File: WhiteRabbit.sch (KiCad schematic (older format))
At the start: 52 parts, among them U13 LP5951MF-3.0/NOPB, U14 LM336M-2.5, U16 AD5662BRMZ-1, U19 AD5662BRMZ-1, U20 CDCM61004RHBT, Y1 OSC_25MHZ_RAKON_IVT3205CR, Y2 VM53S3-25.000-2.5/-30+75, Y3 OSC_20MHZ_IQD_LFVCXO026156

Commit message: DDR terminations changed, HTML BoM with variant added
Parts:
- removed R101, R102, R95, R96, R97, R98, R99: DNP, Resistors SMD:RESC1005X40N, symbol AMC_FMC_Carrier-PcbDoc-rescue:R-Device
- added R101, R102, R95, R96, R97, R98, R99: R0402_0R_JUMPER, RESC1005X40N, symbol Resistors_SMD:R0402_0R_JUMPER
- Y1: config (none) -> dnf

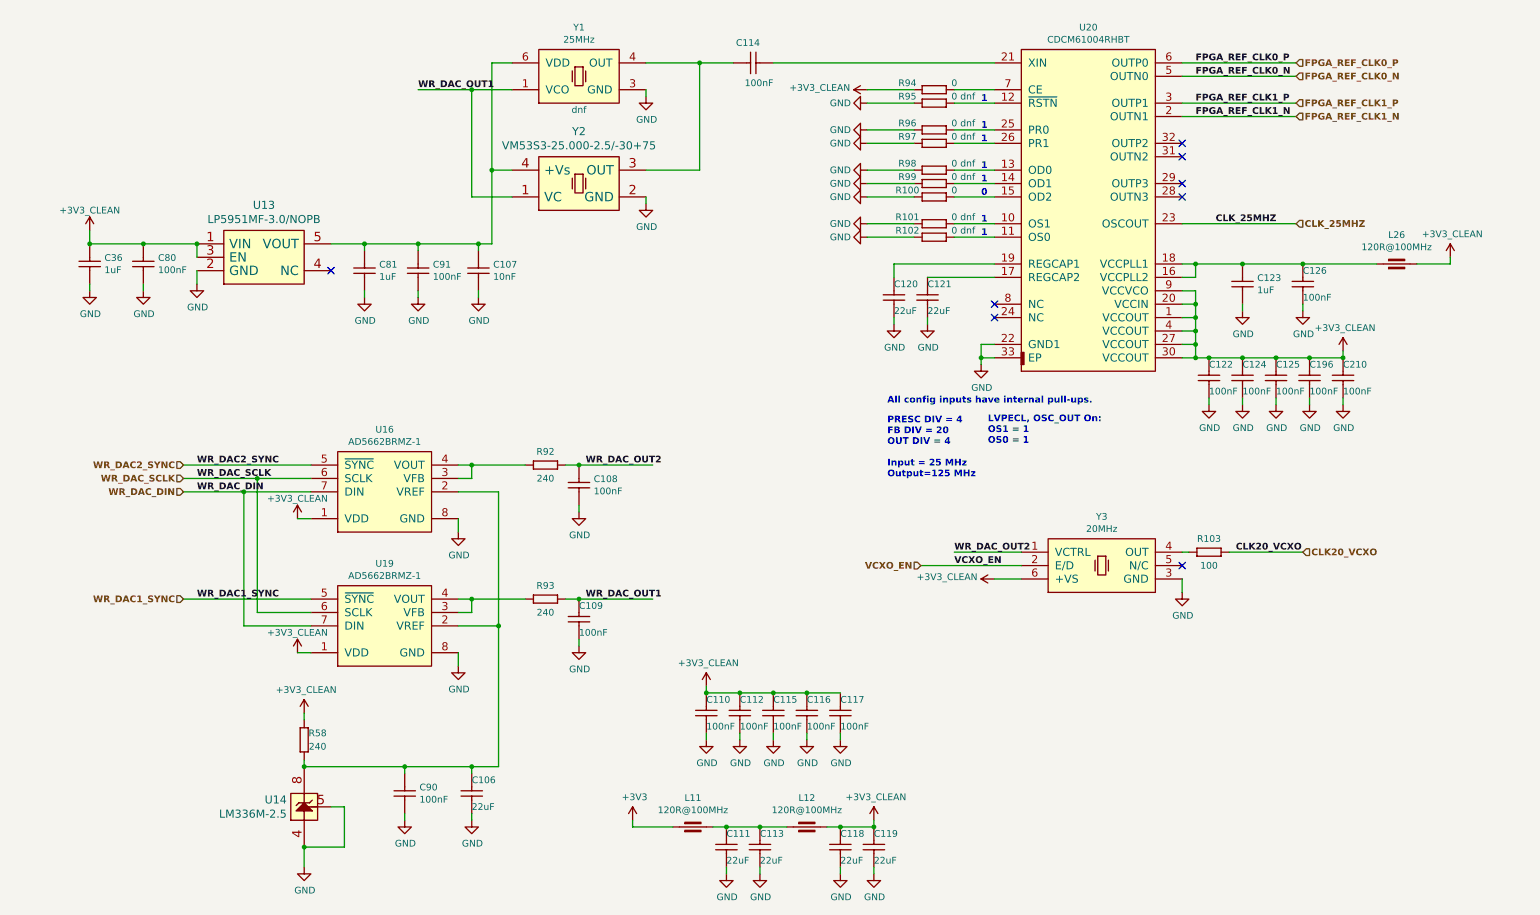
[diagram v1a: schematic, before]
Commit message: SW2 placement changed, BOM cleared, FPGA boot, less ERC errors and wornings
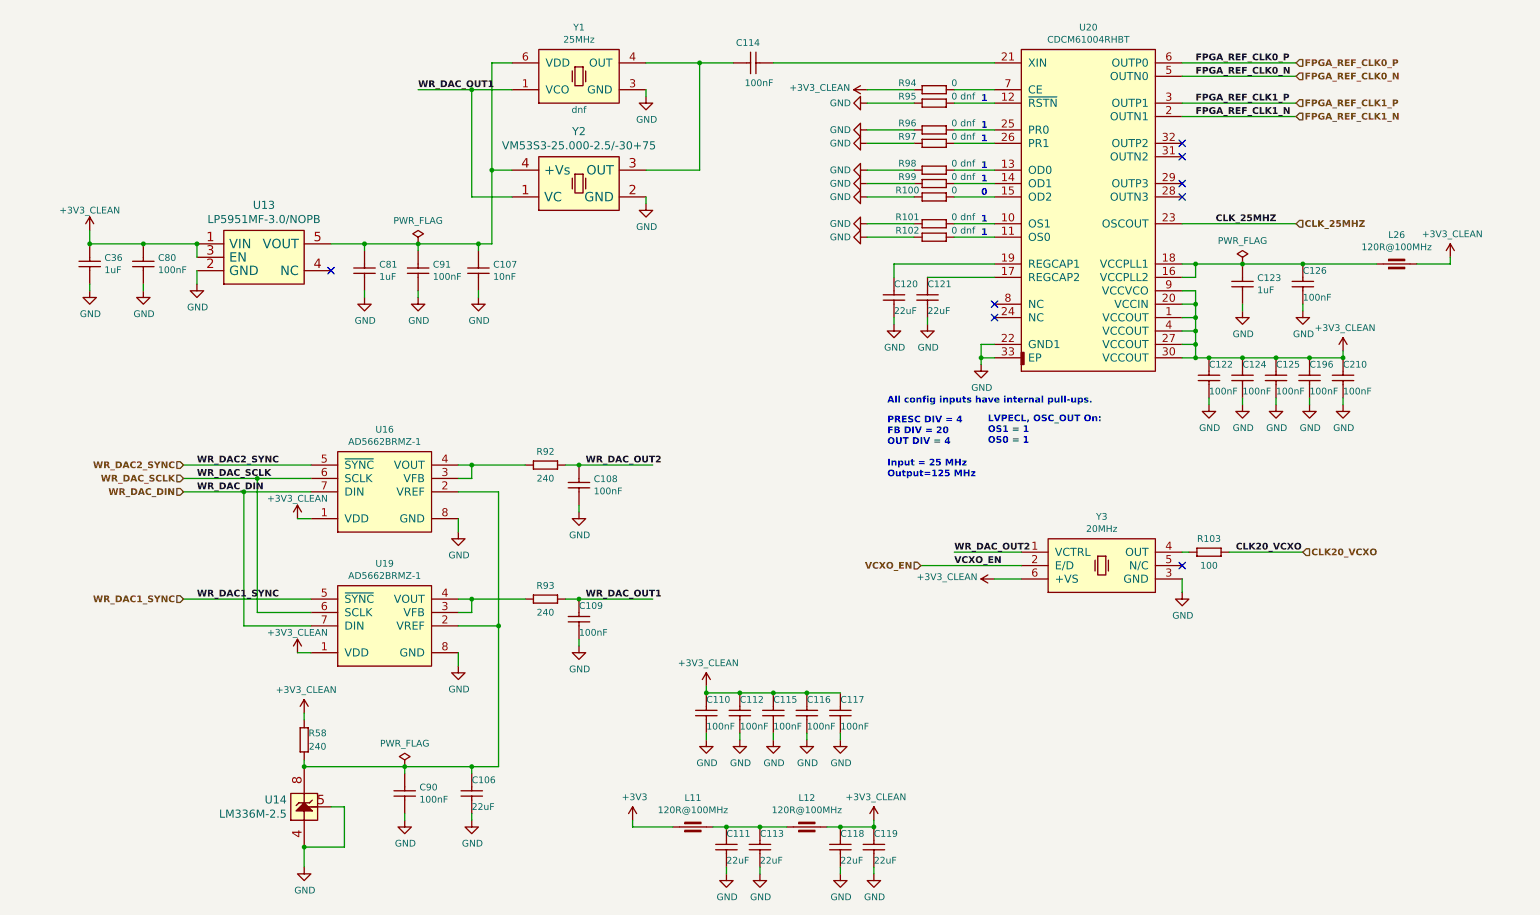
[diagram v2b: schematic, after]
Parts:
- U19: footprint SOP65P490X110-8N -> ICs And Semiconductors SMD:SOP65P490X110-8N
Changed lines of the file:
@@
-$EndComp
-$Comp
-L Analog_&_Interface:AD5662BRMZ-1 U19
-U 1 1 5C5A41A5
-P 2550 5150
-F 0 "U19" H 2900 5315 50  0000 C CNN
-F 1 "AD5662BRMZ-1" H 2900 5224 50  0000 C CNN
-F 2 "SOP65P490X110-8N" H 2550 3460 60  0001 L CNN
-F 3 "\\\\cern.ch\\dfs\\Applications\\Altium\\Datasheets\\AD5662BRMZ-1.pdf" H 2550 4180 60  0001 L CNN
-F 4 "AD5662BRMZ-1" H 2550 4090 60  0001 L CNN "Part Number"
-F 5 "AD5662" H 2550 4000 60  0001 L CNN "Library Ref"
-F 6 "SchLib\\Analog & Interface.SchLib" H 2550 3910 60  0001 L CNN "Library Path"
-F 7 "=Device" H 2550 3820 60  0001 L CNN "Comment"
-F 8 "Standard" H 2550 3730 60  0001 L CNN "Component Kind"
-F 9 "Standard" H 2550 3640 60  0001 L CNN "Component Type"
-F 10 "AD5662BRMZ-1" H 2550 3550 60  0001 L CNN "Device"
-F 11 "SOP, 0.65mm, Pitch; 8 Pin, 3.0mm W X 3.0mm L X 1.10mm H Body, IPC Medium Density" H 2550 3370 60  0001 L CNN "PackageDescription"
-F 12 "~~" H 2550 3280 60  0001 L CNN "Status"
-F 13 "2.7V to 5.5V, 250uA, Rail-to-Rail Output 16-Bit nanoDAC" H 2550 3190 60  0001 L CNN "Part Description"
-F 14 "ANALOG DEVICES" H 2550 3100 60  0001 L CNN "Manufacturer"
-F 15 "AD5662BRMZ-1" H 2550 3010 60  0001 L CNN "Manufacturer Part Number"
-F 16 "8" H 2550 2920 60  0001 L CNN "Pin Count"
-F 17 "MSOP8" H 2550 2830 60  0001 L CNN "Case"
-F 18 "Yes" H 2550 2740 60  0001 L CNN "Mounted"
-F 19 "No" H 2550 2650 60  0001 L CNN "Socket"
-F 20 "Yes" H 2550 2560 60  0001 L CNN "SMD"
-F 21 "No" H 2550 2470 60  0001 L CNN "PressFit"
-F 22 "No" H 2550 2380 60  0001 L CNN "Sense"
-F 23 "~~" H 2550 2290 60  0001 L CNN "Sense Comment"
-F 24 "No" H 2550 2200 60  0001 L CNN "Bonding"
-F 25 "~~" H 2550 2110 60  0001 L CNN "Status Comment"
-F 26 "1.1mm" H 2550 2020 60  0001 L CNN "ComponentHeight"
-F 27 "PcbLib\\ICs And Semiconductors SMD.PcbLib" H 2550 1930 60  0001 L CNN "Footprint Path"
-F 28 "SOP65P490X110-8N" H 2550 1840 60  0001 L CNN "Footprint Ref"
-F 29 "CERN DEM JLC" H 2550 1750 60  0001 L CNN "Author"
-F 30 "\\\\cern.ch\\dfs\\Applications\\Altium\\Datasheets\\AD5662BRMZ-1.pdf" H 2550 1660 60  0001 L CNN "HelpURL"
-F 31 "~~" H 2550 1570 60  0001 L CNN "ComponentLink1URL"
-F 32 "~~" H 2550 1480 60  0001 L CNN "ComponentLink2URL"
-F 33 "~~" H 2550 1390 60  0001 L CNN "ComponentLink2Description"
-F 34 "~~" H 2550 1300 60  0001 L CNN "ComponentLink1Description"
-F 35 "01/10/11 00:00:00" H 2550 1210 60  0001 L CNN "CreateDate"
-F 36 "01/10/11 00:00:00" H 2550 1120 60  0001 L CNN "LatestRevisionDate"
-F 37 "ICs And Semiconductors SMD" H 2550 1030 60  0001 L CNN "Library Name"
-F 38 "This work is licensed under the Creative Commons CC-BY-SA 4.0 License. To the extent that circuit schematics that use Licensed Material can be considered to be ‘Adapted Material’, then the copyright holder waives article 3.b of the license with respect to these schematics." H 2550 940 60  0001 L CNN "License"
-	1    2550 5150
-	1    0    0    -1
 $EndComp
 $Comp
@@
 	1    0    0    -1
 $EndComp
+$Comp
+L power:PWR_FLAG #FLG?
+U 1 1 5D1ECBBF
+P 3150 2600
+AR Path="/5BABAC65/5D1ECBBF" Ref="#FLG?"  Part="1"
+AR Path="/5C16BF13/5D1ECBBF" Ref="#FLG0113"  Part="1"
+F 0 "#FLG0113" H 3150 2675 50  0001 C CNN
+F 1 "PWR_FLAG" H 3150 2773 50  0000 C CNN
+F 2 "" H 3150 2600 50  0001 C CNN
+F 3 "~" H 3150 2600 50  0001 C CNN
+	1    3150 2600
+	1    0    0    -1
+$EndComp
+$Comp
+L power:PWR_FLAG #FLG?
+U 1 1 5D1F3792
+P 9300 2750
+AR Path="/5BABAC65/5D1F3792" Ref="#FLG?"  Part="1"
+AR Path="/5C16BF13/5D1F3792" Ref="#FLG0114"  Part="1"
+F 0 "#FLG0114" H 9300 2825 50  0001 C CNN
+F 1 "PWR_FLAG" H 9300 2923 50  0000 C CNN
+F 2 "" H 9300 2750 50  0001 C CNN
+F 3 "~" H 9300 2750 50  0001 C CNN
+	1    9300 2750
+	1    0    0    -1
+$EndComp
+$Comp
+L power:PWR_FLAG #FLG?
+U 1 1 5D1FA4F7
+P 3050 6500
+AR Path="/5BABAC65/5D1FA4F7" Ref="#FLG?"  Part="1"
+AR Path="/5C16BF13/5D1FA4F7" Ref="#FLG0115"  Part="1"
+F 0 "#FLG0115" H 3050 6575 50  0001 C CNN
+F 1 "PWR_FLAG" H 3050 6673 50  0000 C CNN
+F 2 "" H 3050 6500 50  0001 C CNN
+F 3 "~" H 3050 6500 50  0001 C CNN
+	1    3050 6500
+	1    0    0    -1
+$EndComp
+$Comp
+L Analog_&_Interface:AD5662BRMZ-1 U19
+U 1 1 5D741523
+P 2550 5150
+F 0 "U19" H 2900 5315 50  0000 C CNN
+F 1 "AD5662BRMZ-1" H 2900 5224 50  0000 C CNN
+F 2 "ICs And Semiconductors SMD:SOP65P490X110-8N" H 2550 3460 60  0001 L CNN
+F 3 "" H 2550 4180 60  0001 L CNN
+F 4 "AD5662BRMZ-1" H 2550 4090 60  0001 L CNN "Part Number"
+F 5 "AD5662" H 2550 4000 60  0001 L CNN "Library Ref"
+F 6 "SchLib\\Analog & Interface.SchLib" H 2550 3910 60  0001 L CNN "Library Path"
+F 7 "=Device" H 2550 3820 60  0001 L CNN "Comment"
+F 8 "Standard" H 2550 3730 60  0001 L CNN "Component Kind"
+F 9 "Standard" H 2550 3640 60  0001 L CNN "Component Type"
+F 10 "AD5662BRMZ-1" H 2550 3550 60  0001 L CNN "Device"
+F 11 "SOP, 0.65mm, Pitch; 8 Pin, 3.0mm W X 3.0mm L X 1.10mm H Body, IPC Medium Density" H 2550 3370 60  0001 L CNN "PackageDescription"
+F 12 "~~" H 2550 3280 60  0001 L CNN "Status"
+F 13 "2.7V to 5.5V, 250uA, Rail-to-Rail Output 16-Bit nanoDAC" H 2550 3190 60  0001 L CNN "Part Description"
+F 14 "ANALOG DEVICES" H 2550 3100 60  0001 L CNN "Manufacturer"
+F 15 "AD5662BRMZ-1" H 2550 3010 60  0001 L CNN "Manufacturer Part Number"
+F 16 "8" H 2550 2920 60  0001 L CNN "Pin Count"
+F 17 "MSOP8" H 2550 2830 60  0001 L CNN "Case"
+F 18 "Yes" H 2550 2740 60  0001 L CNN "Mounted"
+F 19 "No" H 2550 2650 60  0001 L CNN "Socket"
+F 20 "Yes" H 2550 2560 60  0001 L CNN "SMD"
+F 21 "No" H 2550 2470 60  0001 L CNN "PressFit"
+F 22 "No" H 2550 2380 60  0001 L CNN "Sense"
+F 23 "~~" H 2550 2290 60  0001 L CNN "Sense Comment"
+F 24 "No" H 2550 2200 60  0001 L CNN "Bonding"
+F 25 "~~" H 2550 2110 60  0001 L CNN "Status Comment"
+F 26 "1.1mm" H 2550 2020 60  0001 L CNN "ComponentHeight"
+F 27 "PcbLib\\ICs And Semiconductors SMD.PcbLib" H 2550 1930 60  0001 L CNN "Footprint Path"
+F 28 "SOP65P490X110-8N" H 2550 1840 60  0001 L CNN "Footprint Ref"
+F 29 "CERN DEM JLC" H 2550 1750 60  0001 L CNN "Author"
+F 30 "\\\\cern.ch\\dfs\\Applications\\Altium\\Datasheets\\AD5662BRMZ-1.pdf" H 2550 1660 60  0001 L CNN "HelpURL"
+F 31 "~~" H 2550 1570 60  0001 L CNN "ComponentLink1URL"
+F 32 "~~" H 2550 1480 60  0001 L CNN "ComponentLink2URL"
+F 33 "~~" H 2550 1390 60  0001 L CNN "ComponentLink2Description"
+F 34 "~~" H 2550 1300 60  0001 L CNN "ComponentLink1Description"
+F 35 "01/10/11 00:00:00" H 2550 1210 60  0001 L CNN "CreateDate"
+F 36 "01/10/11 00:00:00" H 2550 1120 60  0001 L CNN "LatestRevisionDate"
+F 37 "ICs And Semiconductors SMD" H 2550 1030 60  0001 L CNN "Library Name"
+F 38 "This work is licensed under the Creative Commons CC-BY-SA 4.0 License. To the extent that circuit schematics that use Licensed Material can be considered to be ‘Adapted Material’, then the copyright holder waives article 3.b of the license with respect to these schematics." H 2550 940 60  0001 L CNN "License"
+	1    2550 5150
+	1    0    0    -1
+$EndComp

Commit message: BOM updated, 25MHz clock level fixed
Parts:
- U13: symbol AMC_FMC_Carrier-PcbDoc-rescue:LP5951-clocks-SchDoc-cache -> AMC_FMC_Carrier-PcbDoc-rescue:LP5951-clocks-SchDoc-cache-AMC_FMC_Carrier-PcbDoc-rescue
- U14: symbol AMC_FMC_Carrier-PcbDoc-rescue:LM336M-2.5-clocks-SchDoc-cache -> AMC_FMC_Carrier-PcbDoc-rescue:LM336M-2.5-clocks-SchDoc-cache-AMC_FMC_Carrier-PcbDoc-rescue
- Y2: symbol AMC_FMC_Carrier-PcbDoc-rescue:Oscillator_1VC_2GND_3OUT_4+Vs-clocks-SchDoc-cache -> AMC_FMC_Carrier-PcbDoc-rescue:Oscillator_1VC_2GND_3OUT_4+Vs-clocks-SchDoc-cache-AMC_FMC_Carrier-PcbDoc-rescue
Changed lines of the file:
@@
 	3750 4450 3750 5450
 $Comp
-L AMC_FMC_Carrier-PcbDoc-rescue:LM336M-2.5-clocks-SchDoc-cache U14
+L AMC_FMC_Carrier-PcbDoc-rescue:LM336M-2.5-clocks-SchDoc-cache-AMC_FMC_Carrier-PcbDoc-rescue U14
 U 1 1 5C21F363
 P 2200 6900
@@
 	8850 5100 8850 5200
 $Comp
-L AMC_FMC_Carrier-PcbDoc-rescue:+3V3_CLEAN-powerMG #PWR0175
+L AMC_FMC_Carrier-PcbDoc-rescue:+3V3_CLEAN-powerMG-AMC_FMC_Carrier-PcbDoc-rescue #PWR0175
 U 1 1 5C2DA97A
 P 2300 6100
@@
 $EndComp
 $Comp
-L AMC_FMC_Carrier-PcbDoc-rescue:+3V3_CLEAN-powerMG #PWR0174
+L AMC_FMC_Carrier-PcbDoc-rescue:+3V3_CLEAN-powerMG-AMC_FMC_Carrier-PcbDoc-rescue #PWR0174
 U 1 1 5C2DA9DF
 P 2250 5650
@@
 $EndComp
 $Comp
-L AMC_FMC_Carrier-PcbDoc-rescue:+3V3_CLEAN-powerMG #PWR0209
+L AMC_FMC_Carrier-PcbDoc-rescue:+3V3_CLEAN-powerMG-AMC_FMC_Carrier-PcbDoc-rescue #PWR0209
 U 1 1 5C2DD28D
 P 7450 5100
@@
 $EndComp
 $Comp
-L AMC_FMC_Carrier-PcbDoc-rescue:+3V3_CLEAN-powerMG #PWR0173
+L AMC_FMC_Carrier-PcbDoc-rescue:+3V3_CLEAN-powerMG-AMC_FMC_Carrier-PcbDoc-rescue #PWR0173
 U 1 1 5C2DDAC4
 P 2250 4650
@@
 CLK20_VCXO
 $Comp
-L AMC_FMC_Carrier-PcbDoc-rescue:LP5951-clocks-SchDoc-cache U13
+L AMC_FMC_Carrier-PcbDoc-rescue:LP5951-clocks-SchDoc-cache-AMC_FMC_Carrier-PcbDoc-rescue U13
 U 1 1 5C2E75E7
 P 1700 2500
@@
 $EndComp
 $Comp
-L AMC_FMC_Carrier-PcbDoc-rescue:+3V3_CLEAN-powerMG #PWR0169
+L AMC_FMC_Carrier-PcbDoc-rescue:+3V3_CLEAN-powerMG-AMC_FMC_Carrier-PcbDoc-rescue #PWR0169
 U 1 1 5C2EF25E
 P 700 2500
@@
 $EndComp
 $Comp
-L AMC_FMC_Carrier-PcbDoc-rescue:Oscillator_1VC_2GND_3OUT_4+Vs-clocks-SchDoc-cache Y2
+L AMC_FMC_Carrier-PcbDoc-rescue:Oscillator_1VC_2GND_3OUT_4+Vs-clocks-SchDoc-cache-AMC_FMC_Carrier-PcbDoc-rescue Y2
 U 1 1 5C2F3070
 P 4050 1950
@@
 $EndComp
 $Comp
-L AMC_FMC_Carrier-PcbDoc-rescue:+3V3_CLEAN-powerMG #PWR0206
+L AMC_FMC_Carrier-PcbDoc-rescue:+3V3_CLEAN-powerMG-AMC_FMC_Carrier-PcbDoc-rescue #PWR0206
 U 1 1 5C33B37A
 P 6550 6900
@@
 	6300 6250 6300 6300
 $Comp
-L AMC_FMC_Carrier-PcbDoc-rescue:+3V3_CLEAN-powerMG #PWR0189
+L AMC_FMC_Carrier-PcbDoc-rescue:+3V3_CLEAN-powerMG-AMC_FMC_Carrier-PcbDoc-rescue #PWR0189
 U 1 1 5C3A12D5
 P 5300 5900
@@
 	5300 5900 5300 5950
 $Comp
-L AMC_FMC_Carrier-PcbDoc-rescue:+3V3_CLEAN-powerMG #PWR0211
+L AMC_FMC_Carrier-PcbDoc-rescue:+3V3_CLEAN-powerMG-AMC_FMC_Carrier-PcbDoc-rescue #PWR0211
 U 1 1 5C8A0C88
 P 6500 1450
@@
 	10050 3750 10050 3800
 $Comp
-L AMC_FMC_Carrier-PcbDoc-rescue:+3V3_CLEAN-powerMG #PWR0399
+L AMC_FMC_Carrier-PcbDoc-rescue:+3V3_CLEAN-powerMG-AMC_FMC_Carrier-PcbDoc-rescue #PWR0399
 U 1 1 5D15AFE0
 P 10050 3400
@@
 NoConn ~ 2500 2800
 $Comp
-L AMC_FMC_Carrier-PcbDoc-rescue:+3V3_CLEAN-powerMG #PWR0401
+L AMC_FMC_Carrier-PcbDoc-rescue:+3V3_CLEAN-powerMG-AMC_FMC_Carrier-PcbDoc-rescue #PWR0401
 U 1 1 5D19EDBE
 P 10850 2700

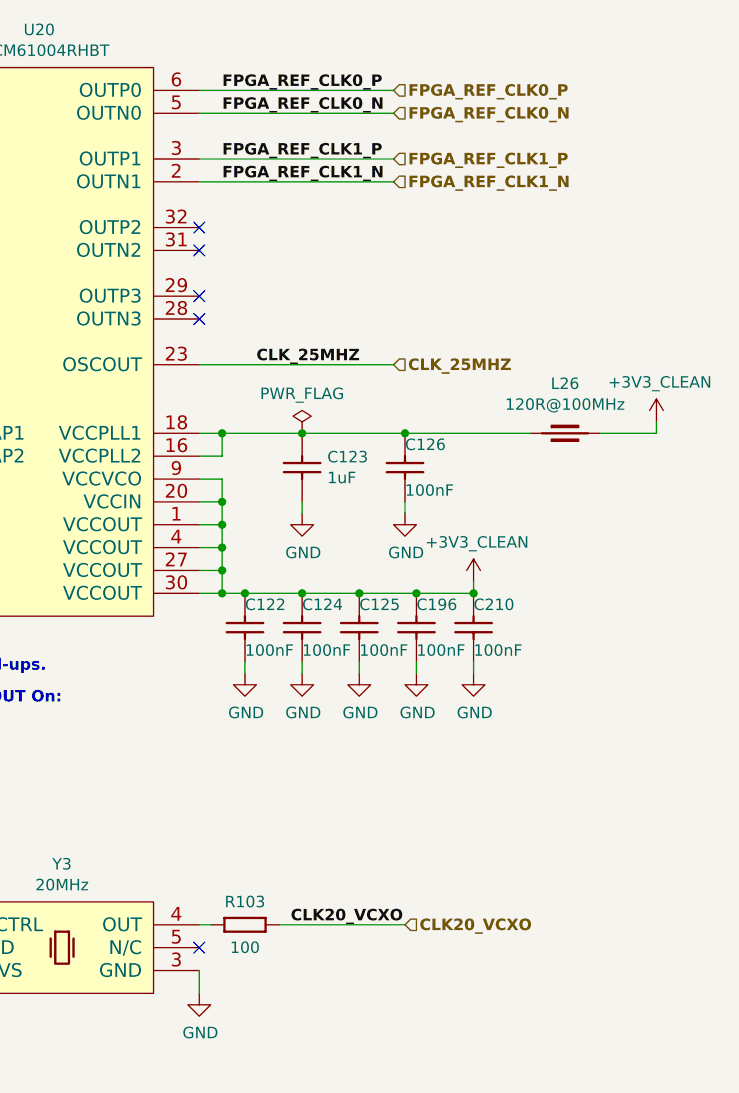
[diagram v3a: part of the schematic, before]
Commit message: new FMC JTAG chain connected to MMC GPIO
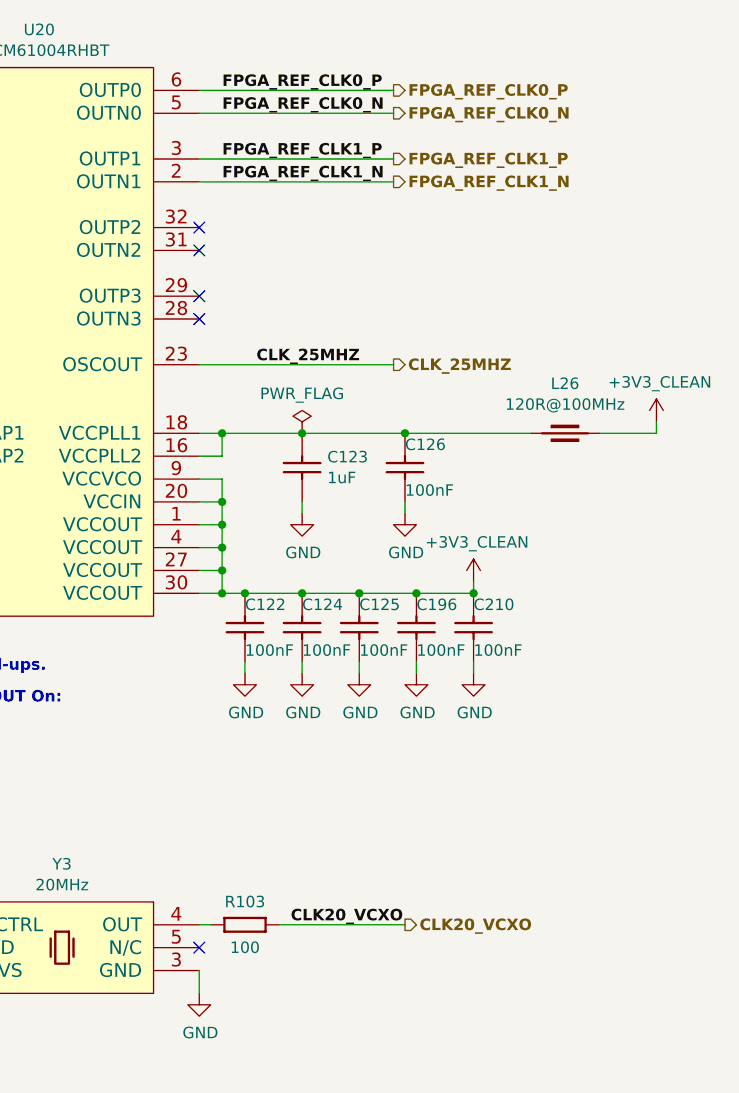
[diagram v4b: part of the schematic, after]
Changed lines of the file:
@@
 Text HLabel 1400 5250 0    50   Input ~ 10
 WR_DAC1_SYNC
-Text HLabel 9750 4900 2    50   Input ~ 10
+Text HLabel 9750 4900 2    50   Output ~ 10
 CLK20_VCXO
 Wire Wire Line
@@
 Text Label 8950 1650 0    50   ~ 10
 FPGA_REF_CLK1_N
-Text HLabel 9700 1250 2    50   Input ~ 10
+Text HLabel 9700 1250 2    50   Output ~ 10
 FPGA_REF_CLK0_P
-Text HLabel 9700 1350 2    50   Input ~ 10
+Text HLabel 9700 1350 2    50   Output ~ 10
 FPGA_REF_CLK0_N
-Text HLabel 9700 1550 2    50   Input ~ 10
+Text HLabel 9700 1550 2    50   Output ~ 10
 FPGA_REF_CLK1_P
-Text HLabel 9700 1650 2    50   Input ~ 10
+Text HLabel 9700 1650 2    50   Output ~ 10
 FPGA_REF_CLK1_N
 Wire Wire Line
@@
 Wire Wire Line
 	9700 2450 8850 2450
-Text HLabel 9700 2450 2    50   Input ~ 10
+Text HLabel 9700 2450 2    50   Output ~ 10
 CLK_25MHZ
 Text Label 9100 2450 0    50   ~ 10

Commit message: BOM configuration file edited, updated Marble picture, some components part number changed
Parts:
- U13: Manufacturer Part Number (none) -> LP5951MF-3.0/NOPB; PN LP5951MF-3.0/NOPB -> (none)
- U14: Manufacturer Part Number (none) -> LM336M-2.5
- Y2: Manufacturer Part Number (none) -> VM53S3-25.000-2.5/-30+75; PN VM53S3-25.000-2.5/-30+75 -> (none)
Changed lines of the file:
@@
 F 2 "ICs And Semiconductors SMD:SOIC127P600X175-8N" H 2200 6900 60  0001 C CNN
 F 3 "" H 2200 6900 60  0000 C CNN
+F 4 "LM336M-2.5" V 2200 6900 50  0001 C CNN "Manufacturer Part Number"
 	1    2200 6900
 	0    -1   -1   0
@@
 F 2 "ICs And Semiconductors SMD:SOT95P284X122-5N" H 2000 2583 60  0001 C CNN
 F 3 "" H 1700 2500 60  0000 C CNN
-F 4 "LP5951MF-3.0/NOPB" H 1700 2500 50  0001 C CNN "PN"
+F 4 "LP5951MF-3.0/NOPB" H 1700 2500 50  0001 C CNN "Manufacturer Part Number"
 	1    1700 2500
 	1    0    0    -1
@@
 F 2 "ICs And Semiconductors SMD:OSCCC320X500X160-4N" H 4350 2033 60  0001 C CNN
 F 3 "" H 4050 1950 60  0000 C CNN
-F 4 "VM53S3-25.000-2.5/-30+75" H 4050 1950 50  0001 C CNN "PN"
+F 4 "VM53S3-25.000-2.5/-30+75" H 4050 1950 50  0001 C CNN "Manufacturer Part Number"
 	1    4050 1950
 	1    0    0    -1
